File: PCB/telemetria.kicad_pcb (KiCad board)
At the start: 2 copper layers, 81 x 50 mm, 8 parts, among them P12 CONN_01X04, P4 CONN_01X07, P7 CONN_01X07, P9 CONN_01X04, U2 RFM95W-868S2

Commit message: Finished telemtry PCB
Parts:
- A1: footprint LoRa:SMA_Conn_Ant -> smd:AMPHENOL_901-144
- moved A1 9.35 mm to (128.5, 82.0), turned to 0 degrees
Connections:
- A1 pad 1: GND -> Net-(A1-Pad1)
- A1 pad 2: Net-(A1-Pad2) -> GND
- U2 pad 9: Net-(A1-Pad2) -> Net-(A1-Pad1)
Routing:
- net +BATT: track 0.00 -> 69.7 mm, vias 0 -> 1
- net INT0: track 0.00 -> 36.2 mm, vias 0 -> 1
- net Net-(A1-Pad1): track 0.00 -> 29.4 mm
- net GND: track 10.3 -> 37.9 mm
- net S_TX: track 0.00 -> 25.3 mm
- net S_RX: track 0.00 -> 21.9 mm
- net SCK: track 0.00 -> 11.2 mm, vias 0 -> 1
- net MOSI: track 0.00 -> 8.86 mm
- net MISO: track 0.00 -> 8.27 mm
- net RST: track 0.00 -> 8.12 mm
- net NSS: track 0.00 -> 7.89 mm
- added copper zone on F.Cu, net GND

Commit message: Fix PCBs
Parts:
- MODULE1: value L80-M39 -> L80-GPS
- U2: value RFM95W-868S2 -> RFM95W-LoRa
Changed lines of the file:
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@@
-(kicad_pcb (version 4) (host pcbnew 4.0.0-rc1-stable)
+(kicad_pcb (version 4) (host pcbnew 4.0.2+dfsg1-stable)
   (general
     (links 24)
@@
   )
   (layers
-    (0 F.Cu signal)
-    (31 B.Cu signal)
+    (0 F.Cu signal hide)
+    (31 B.Cu signal hide)
     (32 B.Adhes user)
     (33 F.Adhes user)
@@
       (effects (font (size 0.77216 0.77216) (thickness 0.138988)) (justify left bottom))
     )
-    (fp_text value RFM95W-868S2 (at -8.1 8.7) (layer F.SilkS)
-      (effects (font (size 0.38608 0.38608) (thickness 0.038608)) (justify left bottom))
+    (fp_text value RFM95W-LoRa (at -7.55 9.95) (layer F.SilkS)
+      (effects (font (size 1 1) (thickness 0.15)) (justify left bottom))
     )
     (fp_line (start -8 -8) (end 8 -8) (layer Dwgs.User) (width 0.127))
@@
     (solder_mask_margin 0.1)
     (attr smd)
-    (fp_text reference MODULE1 (at -5.46 -9.635 180) (layer F.SilkS)
+    (fp_text reference MODULE1 (at -5.46 -9.635 180) (layer F.Fab)
       (effects (font (size 1 1) (thickness 0.05)))
     )
-    (fp_text value L80-M39 (at 4.860978 -9.966894 360) (layer F.SilkS)
-      (effects (font (size 1 1) (thickness 0.05)))
+    (fp_text value L80-GPS (at 3.133668 -9.281494 180) (layer F.SilkS)
+      (effects (font (size 1 1) (thickness 0.15)))
     )
     (fp_line (start 8.033668 -8.211494) (end -7.966332 -8.211494) (layer Dwgs.User) (width 0.254))
@@
     (descr "Through hole pin header")
     (tags "pin header")
-    (fp_text reference P4 (at 0 -5.1) (layer F.SilkS)
-      (effects (font (size 1 1) (thickness 0.15)))
-    )
-    (fp_text value CONN_01X07 (at 0 -3.1) (layer F.Fab)
+    (fp_text reference P4 (at 0.2 -3) (layer F.SilkS)
+      (effects (font (size 1 1) (thickness 0.15)))
+    )
+    (fp_text value CONN_01X07 (at 2.4 7.6 90) (layer F.Fab)
       (effects (font (size 1 1) (thickness 0.15)))
     )
@@
     (descr "Through hole pin header")
     (tags "pin header")
-    (fp_text reference P7 (at 0 -5.1 90) (layer F.SilkS)
+    (fp_text reference P7 (at 0.15 -2.85 90) (layer F.SilkS)
       (effects (font (size 1 1) (thickness 0.15)))
     )
@@
     (at 128.54 82.04)
     (solder_mask_margin 0.1)
-    (fp_text reference A1 (at -0.4826 -5.0546) (layer F.SilkS)
+    (fp_text reference A1 (at -0.4826 -5.0546) (layer F.Fab)
       (effects (font (size 1.64 1.64) (thickness 0.05)))
     )
     (fp_text value ANT (at -0.381 5.5626) (layer F.SilkS)
-      (effects (font (size 1.64 1.64) (thickness 0.05)))
+      (effects (font (size 1 1) (thickness 0.15)))
     )
     (fp_line (start -1.2954 3.5052) (end 1.2954 3.5052) (layer F.SilkS) (width 0.1524))
@@
   (segment (start 113.25 102.65) (end 113.85 102.65) (width 0.25) (layer F.Cu) (net 1))
   (segment (start 97.05 90.65) (end 97.65 90.65) (width 0.25) (layer F.Cu) (net 1))
-  (segment (start 112.6 74.61) (end 111.14 74.61) (width 0.25) (layer F.Cu) (net 2) (status 400000))
-  (segment (start 93.75 88.25) (end 91.6 90.4) (width 0.25) (layer F.Cu) (net 2) (status 800000))
+  (segment (start 112.6 74.61) (end 111.14 74.61) (width 0.25) (layer F.Cu) (net 2))
+  (segment (start 93.75 88.25) (end 91.6 90.4) (width 0.25) (layer F.Cu) (net 2))
   (segment (start 97.5 88.25) (end 93.75 88.25) (width 0.25) (layer F.Cu) (net 2))
   (segment (start 111.14 74.61) (end 97.5 88.25) (width 0.25) (layer F.Cu) (net 2))

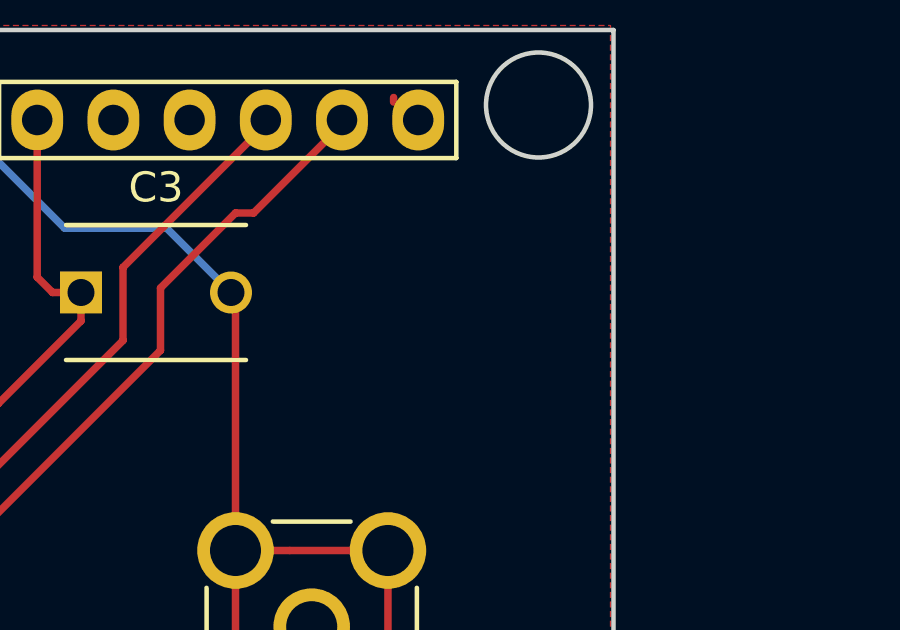
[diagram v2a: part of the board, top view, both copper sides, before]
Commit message: Add logo ElectronicCats
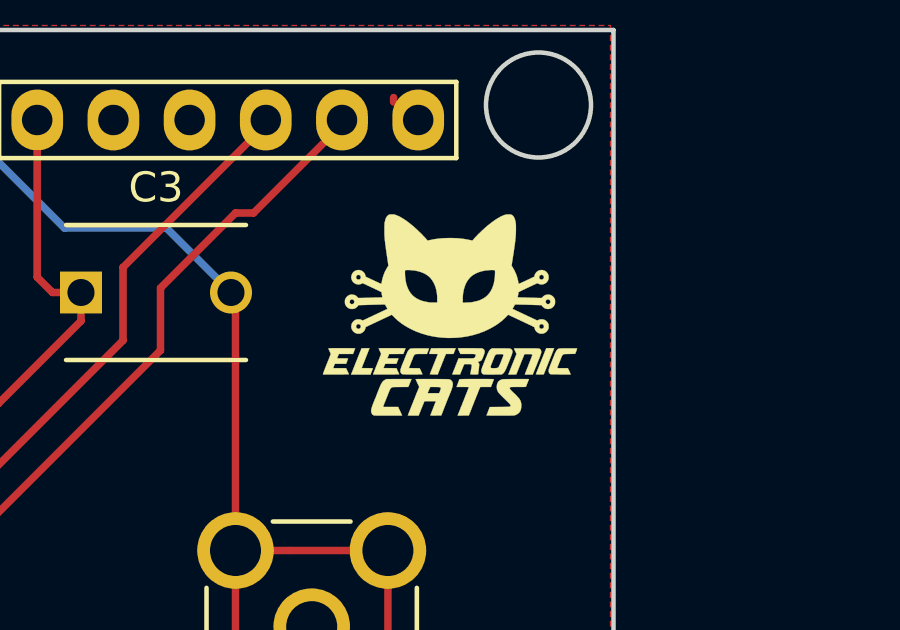
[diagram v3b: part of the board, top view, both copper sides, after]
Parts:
- added G***: LOGO, theinventorhouse:electronic_cats_logo_8x6, F.Cu at (133.2, 71.7)

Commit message: PCB final
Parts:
- added R1: R, Resistors_ThroughHole:Resistor_Horizontal_RM7mm, F.Cu at (103.5, 110.0)
- added R2: R, Resistors_ThroughHole:Resistor_Horizontal_RM7mm, F.Cu at (107.0, 109.9)
- MODULE1: value L80-GPS -> L80-M39
- U2: value RFM95W-LoRa -> RFM95W-868S2
- moved C3 33.1 mm to (91.8, 86.8), turned to 90 degrees
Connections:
- MODULE1 pad 5: Net-(MODULE1-Pad5) -> +BATT
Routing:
- net +BATT: track 69.7 -> 94.8 mm
- net NSS: track 7.89 -> 29.5 mm
- net RST: track 8.12 -> 14.2 mm
- net GND: track 37.9 -> 42.5 mm
- net (no net): track 1.57 -> 0.00 mm
- net INT0: track 36.2 -> 34.9 mm
- net SCK: track 11.2 -> 10.6 mm
- added copper zone on B.Cu, net GND
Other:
- board size 81 x 50 mm -> 50 x 50 mm
- net class +BATT added: clearance 0.2, trace_width 0.5, via_dia 0.6, via_drill 0.4

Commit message: Fix details
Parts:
- added REF**: Symbol_OSHW-Logo_SilkScreen_BIG, Symbols:Symbol_OSHW-Logo_SilkScreen_BIG, B.Cu at (107.0, 59.8)
- turned A1 to 180 degrees
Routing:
- net GND: track 42.5 -> 48.3 mm
- net Net-(A1-Pad1): track 29.4 -> 34.7 mm
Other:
- board text added: "Telemetry & GPS Board"
